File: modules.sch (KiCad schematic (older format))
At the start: 0 parts

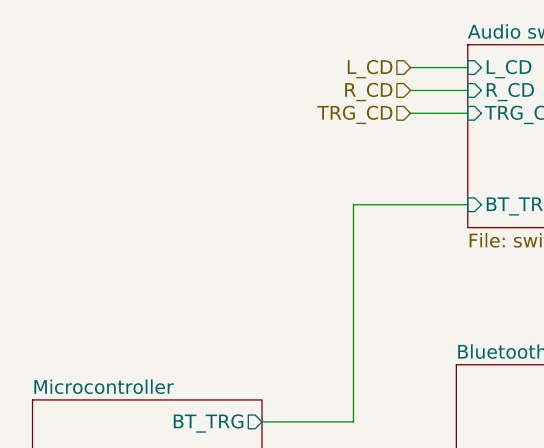
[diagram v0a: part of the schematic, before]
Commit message: Add resistor values to LEDs and a voltage regulator. Has power pin errors still.
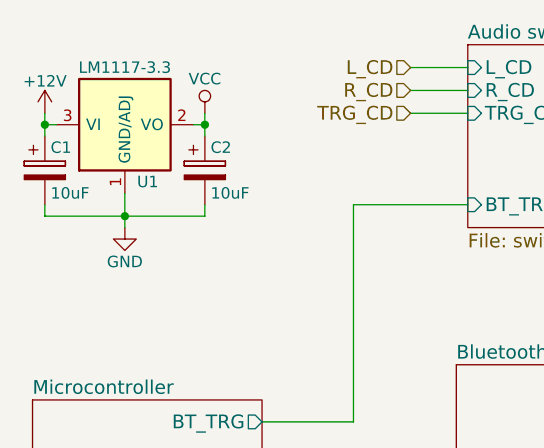
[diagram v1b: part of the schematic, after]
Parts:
- added C1, C2: 10uF, symbol CP
- added U1: LM1117-3.3, symbol LM1117-3.3
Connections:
- new net +12V: C1.1, U1.3 (VI)
- new net GND: C1.2, C2.2, U1.1 (GND/ADJ)
- new net VCC: C2.1, U1.2 (VO), U1.4 (VO)
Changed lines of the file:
@@
 Wire Wire Line
 	4650 4900 5500 4900
+$Comp
+L LM1117-3.3 U1
+U 1 1 59484141
+P 4050 3300
+F 0 "U1" H 4150 3050 50  0000 C CNN
+F 1 "LM1117-3.3" H 4050 3550 50  0000 C CNN
+F 2 "" H 4050 3300 50  0001 C CNN
+F 3 "" H 4050 3300 50  0001 C CNN
+	1    4050 3300
+	1    0    0    -1
+$EndComp
+$Comp
+L GND #PWR07
+U 1 1 59484363
+P 4050 3750
+F 0 "#PWR07" H 4050 3500 50  0001 C CNN
+F 1 "GND" H 4050 3600 50  0000 C CNN
+F 2 "" H 4050 3750 50  0001 C CNN
+F 3 "" H 4050 3750 50  0001 C CNN
+	1    4050 3750
+	1    0    0    -1
+$EndComp
+Wire Wire Line
+	4050 3600 4050 3750
+$Comp
+L +12V #PWR08
+U 1 1 59484575
+P 3700 3250
+F 0 "#PWR08" H 3700 3100 50  0001 C CNN
+F 1 "+12V" H 3700 3390 50  0000 C CNN
+F 2 "" H 3700 3250 50  0001 C CNN
+F 3 "" H 3700 3250 50  0001 C CNN
+	1    3700 3250
+	1    0    0    -1
+$EndComp
+Wire Wire Line
+	3700 3250 3700 3350
+Wire Wire Line
+	3700 3300 3750 3300
+Wire Wire Line
+	4400 3250 4400 3350
+Wire Wire Line
+	4400 3300 4350 3300
+$Comp
+L CP C1
+U 1 1 59484D99
+P 3700 3500
+F 0 "C1" H 3725 3600 50  0000 L CNN
+F 1 "10uF" H 3725 3400 50  0000 L CNN
+F 2 "" H 3738 3350 50  0001 C CNN
+F 3 "" H 3700 3500 50  0001 C CNN
+	1    3700 3500
+	1    0    0    -1
+$EndComp
+$Comp
+L CP C2
+U 1 1 59484E96
+P 4400 3500
+F 0 "C2" H 4425 3600 50  0000 L CNN
+F 1 "10uF" H 4425 3400 50  0000 L CNN
+F 2 "" H 4438 3350 50  0001 C CNN
+F 3 "" H 4400 3500 50  0001 C CNN
+	1    4400 3500
+	1    0    0    -1
+$EndComp
+Wire Wire Line
+	3700 3650 3700 3700
+Wire Wire Line
+	3700 3700 4400 3700
+Connection ~ 4050 3700
+Wire Wire Line
+	4400 3700 4400 3650
+Connection ~ 4400 3300
+Connection ~ 3700 3300
+$Comp
+L VCC #PWR09
+U 1 1 59486886
+P 4400 3250
+F 0 "#PWR09" H 4400 3100 50  0001 C CNN
+F 1 "VCC" H 4400 3400 50  0000 C CNN
+F 2 "" H 4400 3250 50  0001 C CNN
+F 3 "" H 4400 3250 50  0001 C CNN
+	1    4400 3250
+	1    0    0    -1
+$EndComp
 $EndSCHEMATC

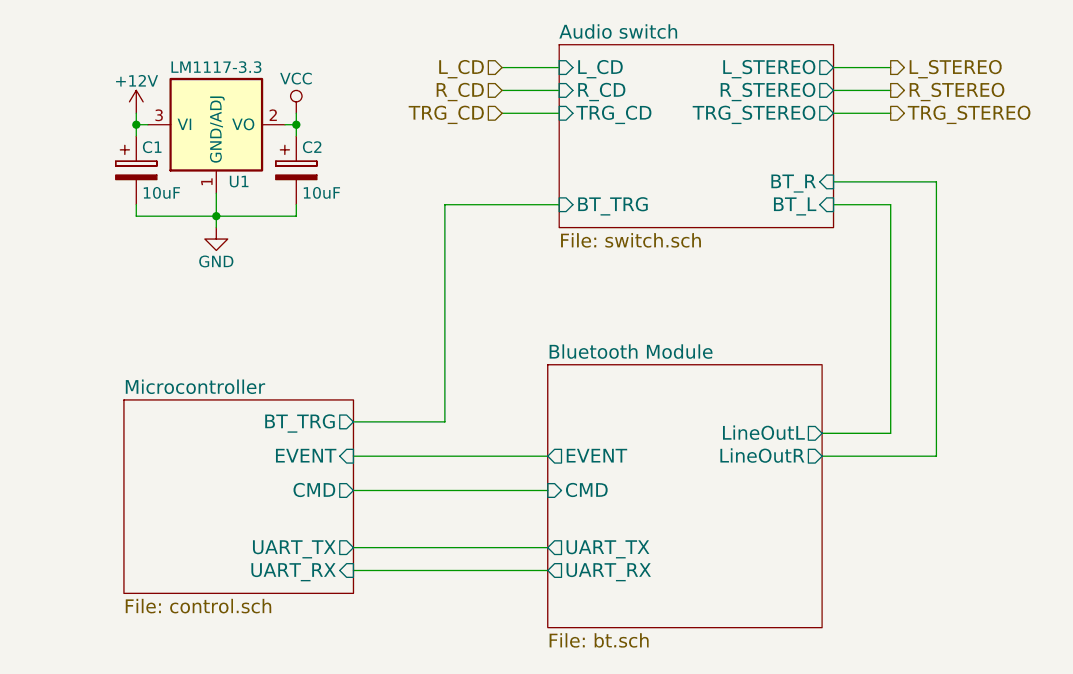
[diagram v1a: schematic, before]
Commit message: Voltage regulator adjustments and tidying
Switch to LD1117 component and add decoupling caps.
Add a decoupling cap to the audio switch
Shift some status LEDs to modules layer
Use ProMini instead of ProMicro
Update BOM
Update netlist
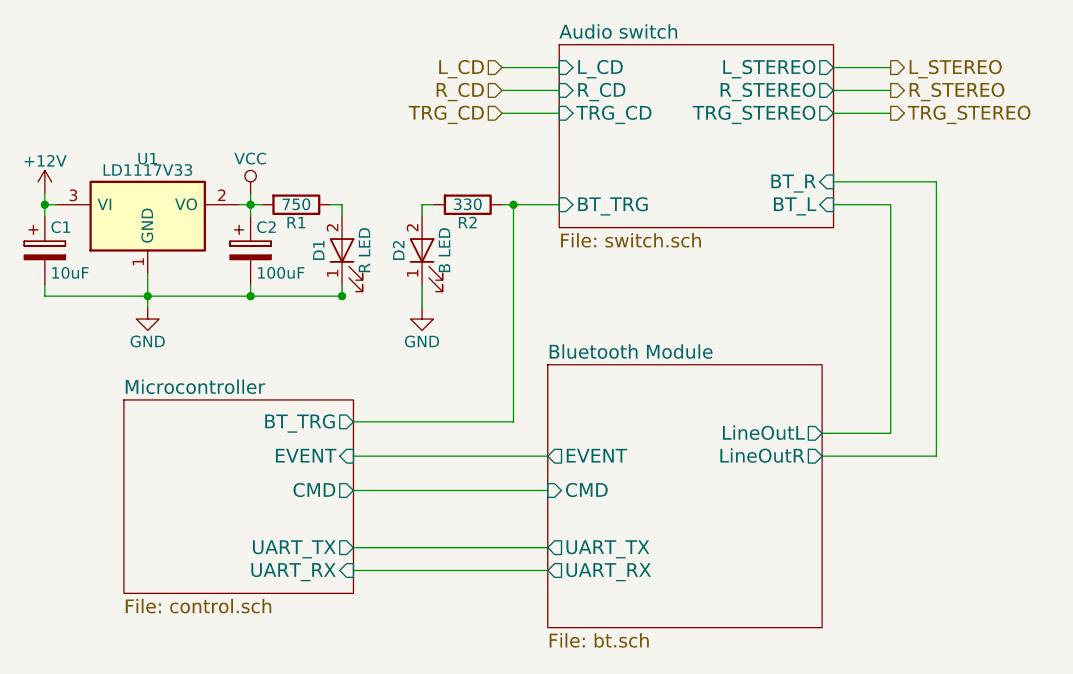
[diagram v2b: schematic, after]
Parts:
- removed U1: LM1117-3.3, symbol LM1117-3.3
- added D1: R LED, LEDs:LED_D3.0mm_Horizontal_O1.27mm_Z2.0mm, symbol LED
- added D2: B LED, LEDs:LED_D3.0mm_Horizontal_O1.27mm_Z2.0mm, symbol LED
- added R1: 750, Resistors_THT:R_Axial_DIN0204_L3.6mm_D1.6mm_P1.90mm_Vertical, symbol R
- added R2: 330, Resistors_THT:R_Axial_DIN0204_L3.6mm_D1.6mm_P1.90mm_Vertical, symbol R
- added U1: LD1117V33, TO_SOT_Packages_THT:TO-220_Vertical, symbol LD1117S33TR
- C1: footprint (none) -> Capacitors_THT:CP_Radial_D4.0mm_P1.50mm
- C2: value 10uF -> 100uF; footprint (none) -> Capacitors_THT:CP_Radial_D4.0mm_P1.50mm
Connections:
- net +12V: now also U1.3 (VI)
- net Audio switch/BT_TRG: now also R2.1
- net GND: now also D1.1 (K), D2.1 (K), U1.1 (GND)
- net VCC: now also R1.2, U1.2 (VO)
- new net: D1.2 (A), R1.1
- new net: D2.2 (A), R2.2
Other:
- moved on the sheet: C1, C2
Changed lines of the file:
@@
 	7200 4750 6700 4750
 Wire Wire Line
-	4650 4600 5050 4600
+	4650 4600 5350 4600
 Wire Wire Line
-	5050 4600 5050 3650
+	5350 4600 5350 3650
 Wire Wire Line
-	5050 3650 5550 3650
+	5300 3650 5550 3650
 Text HLabel 5300 3250 0    60   Input ~ 0
 TRG_CD
@@
 	4650 4900 5500 4900
 $Comp
-L LM1117-3.3 U1
-U 1 1 59484141
-P 4050 3300
-F 0 "U1" H 4150 3050 50  0000 C CNN
-F 1 "LM1117-3.3" H 4050 3550 50  0000 C CNN
-F 2 "" H 4050 3300 50  0001 C CNN
-F 3 "" H 4050 3300 50  0001 C CNN
-	1    4050 3300
-	1    0    0    -1
-$EndComp
-$Comp
 L GND #PWR07
 U 1 1 59484363
-P 4050 3750
-F 0 "#PWR07" H 4050 3500 50  0001 C CNN
-F 1 "GND" H 4050 3600 50  0000 C CNN
-F 2 "" H 4050 3750 50  0001 C CNN
-F 3 "" H 4050 3750 50  0001 C CNN
-	1    4050 3750
+P 3750 4100
+F 0 "#PWR07" H 3750 3850 50  0001 C CNN
+F 1 "GND" H 3750 3950 50  0000 C CNN
+F 2 "" H 3750 4100 50  0001 C CNN
+F 3 "" H 3750 4100 50  0001 C CNN
+	1    3750 4100
 	1    0    0    -1
 $EndComp
 Wire Wire Line
-	4050 3600 4050 3750
+	3750 3950 3750 4100
 $Comp
 L +12V #PWR08
 U 1 1 59484575
-P 3700 3250
-F 0 "#PWR08" H 3700 3100 50  0001 C CNN
-F 1 "+12V" H 3700 3390 50  0000 C CNN
-F 2 "" H 3700 3250 50  0001 C CNN
-F 3 "" H 3700 3250 50  0001 C CNN
-	1    3700 3250
+P 3300 3600
+F 0 "#PWR08" H 3300 3450 50  0001 C CNN
+F 1 "+12V" H 3300 3740 50  0000 C CNN
+F 2 "" H 3300 3600 50  0001 C CNN
+F 3 "" H 3300 3600 50  0001 C CNN
+	1    3300 3600
 	1    0    0    -1
 $EndComp
 Wire Wire Line
-	3700 3250 3700 3350
+	3300 3600 3300 3700
 Wire Wire Line
-	3700 3300 3750 3300
-Wire Wire Line
-	4400 3250 4400 3350
-Wire Wire Line
-	4400 3300 4350 3300
+	4200 3600 4200 3700
 $Comp
 L CP C1
 U 1 1 59484D99
-P 3700 3500
-F 0 "C1" H 3725 3600 50  0000 L CNN
-F 1 "10uF" H 3725 3400 50  0000 L CNN
-F 2 "" H 3738 3350 50  0001 C CNN
-F 3 "" H 3700 3500 50  0001 C CNN
-	1    3700 3500
+P 3300 3850
+F 0 "C1" H 3325 3950 50  0000 L CNN
+F 1 "10uF" H 3325 3750 50  0000 L CNN
+F 2 "Capacitors_THT:CP_Radial_D4.0mm_P1.50mm" H 3338 3700 50  0001 C CNN
+F 3 "" H 3300 3850 50  0001 C CNN
+	1    3300 3850
 	1    0    0    -1
 $EndComp
@@
 L CP C2
 U 1 1 59484E96
-P 4400 3500
-F 0 "C2" H 4425 3600 50  0000 L CNN
-F 1 "10uF" H 4425 3400 50  0000 L CNN
-F 2 "" H 4438 3350 50  0001 C CNN
-F 3 "" H 4400 3500 50  0001 C CNN
-	1    4400 3500
+P 4200 3850
+F 0 "C2" H 4225 3950 50  0000 L CNN
+F 1 "100uF" H 4225 3750 50  0000 L CNN
+F 2 "Capacitors_THT:CP_Radial_D4.0mm_P1.50mm" H 4238 3700 50  0001 C CNN
+F 3 "" H 4200 3850 50  0001 C CNN
+	1    4200 3850
 	1    0    0    -1
 $EndComp
 Wire Wire Line
-	3700 3650 3700 3700
+	3300 4000 3300 4050
+Connection ~ 3750 4050
 Wire Wire Line
-	3700 3700 4400 3700
-Connection ~ 4050 3700
-Wire Wire Line
-	4400 3700 4400 3650
-Connection ~ 4400 3300
-Connection ~ 3700 3300
+	4200 4050 4200 4000
+Connection ~ 4200 3650
+Connection ~ 3300 3650
 $Comp
 L VCC #PWR09
 U 1 1 59486886
-P 4400 3250
-F 0 "#PWR09" H 4400 3100 50  0001 C CNN
-F 1 "VCC" H 4400 3400 50  0000 C CNN
-F 2 "" H 4400 3250 50  0001 C CNN
-F 3 "" H 4400 3250 50  0001 C CNN
-	1    4400 3250
+P 4200 3600
+F 0 "#PWR09" H 4200 3450 50  0001 C CNN
+F 1 "VCC" H 4200 3750 50  0000 C CNN
+F 2 "" H 4200 3600 50  0001 C CNN
+F 3 "" H 4200 3600 50  0001 C CNN
+	1    4200 3600
 	1    0    0    -1
 $EndComp
+$Comp
+L LD1117S33TR U1
+U 1 1 5949FB36
+P 3750 3700
+F 0 "U1" H 3750 3950 50  0000 C CNN
+F 1 "LD1117V33" H 3750 3900 50  0000 C CNN
+F 2 "TO_SOT_Packages_THT:TO-220_Vertical" H 3750 3800 50  0001 C CNN
+F 3 "http://www.st.com/content/ccc/resource/technical/document/datasheet/99/3b/7d/91/91/51/4b/be/CD00000544.pdf/files/CD00000544.pdf/jcr:content/translations/en.CD00000544.pdf" H 3750 3700 50  0001 C CNN
+	1    3750 3700
+	1    0    0    -1
+$EndComp
+Wire Wire Line
+	3350 3650 3300 3650
+Wire Wire Line
+	4150 3650 4250 3650
+$Comp
+L R R1
+U 1 1 594DE951
+P 4400 3650
+F 0 "R1" V 4480 3650 50  0000 C CNN
+F 1 "750" V 4400 3650 50  0000 C CNN
+F 2 "Resistors_THT:R_Axial_DIN0204_L3.6mm_D1.6mm_P1.90mm_Vertical" V 4330 3650 50  0001 C CNN
+F 3 "" H 4400 3650 50  0001 C CNN
+	1    4400 3650
+	0    1    1    0
+$EndComp
+$Comp
+L LED D1
+U 1 1 594DE9F6
+P 4600 3850
+F 0 "D1" H 4600 3950 50  0000 C CNN
+F 1 "R LED" H 4600 3750 50  0000 C CNN
+F 2 "LEDs:LED_D3.0mm_Horizontal_O1.27mm_Z2.0mm" H 4600 3850 50  0001 C CNN
+F 3 "" H 4600 3850 50  0001 C CNN
+	1    4600 3850
+	0    -1   -1   0
+$EndComp
+Wire Wire Line
+	4550 3650 4600 3650
+Wire Wire Line
+	4600 3650 4600 3700
+Wire Wire Line
+	4600 4050 4600 4000
+Connection ~ 4200 4050
+$Comp
+L R R2
+U 1 1 594DF732
+P 5150 3650
+F 0 "R2" V 5230 3650 50  0000 C CNN
+F 1 "330" V 5150 3650 50  0000 C CNN
+F 2 "Resistors_THT:R_Axial_DIN0204_L3.6mm_D1.6mm_P1.90mm_Vertical" V 5080 3650 50  0001 C CNN
+F 3 "" H 5150 3650 50  0001 C CNN
+	1    5150 3650
+	0    1    1    0
+$EndComp
+$Comp
+L LED D2
+U 1 1 594DFA15
+P 4950 3850
+F 0 "D2" H 4950 3950 50  0000 C CNN
+F 1 "B LED" H 4950 3750 50  0000 C CNN
+F 2 "LEDs:LED_D3.0mm_Horizontal_O1.27mm_Z2.0mm" H 4950 3850 50  0001 C CNN
+F 3 "" H 4950 3850 50  0001 C CNN
+	1    4950 3850
+	0    -1   -1   0
+$EndComp
+Connection ~ 5350 3650
+Wire Wire Line
+	5000 3650 4950 3650
+Wire Wire Line
+	4950 3650 4950 3700
+Wire Wire Line
+	4950 4000 4950 4100
+Connection ~ 4600 4050
+$Comp
+L GND #PWR010
+U 1 1 594E013B
+P 4950 4100
+F 0 "#PWR010" H 4950 3850 50  0001 C CNN
+F 1 "GND" H 4950 3950 50  0000 C CNN
+F 2 "" H 4950 4100 50  0001 C CNN
+F 3 "" H 4950 4100 50  0001 C CNN
+	1    4950 4100
+	1    0    0    -1
+$EndComp
+Wire Wire Line
+	3300 4050 4600 4050
 $EndSCHEMATC
